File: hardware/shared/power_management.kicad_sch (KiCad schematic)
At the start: 32 parts, among them J3 FH12-12S-0.5SH(55), J4 1S Li-Po, Q1 AO3400A, U2 nPM1300-QEAA, U7 TPS63900DSKR

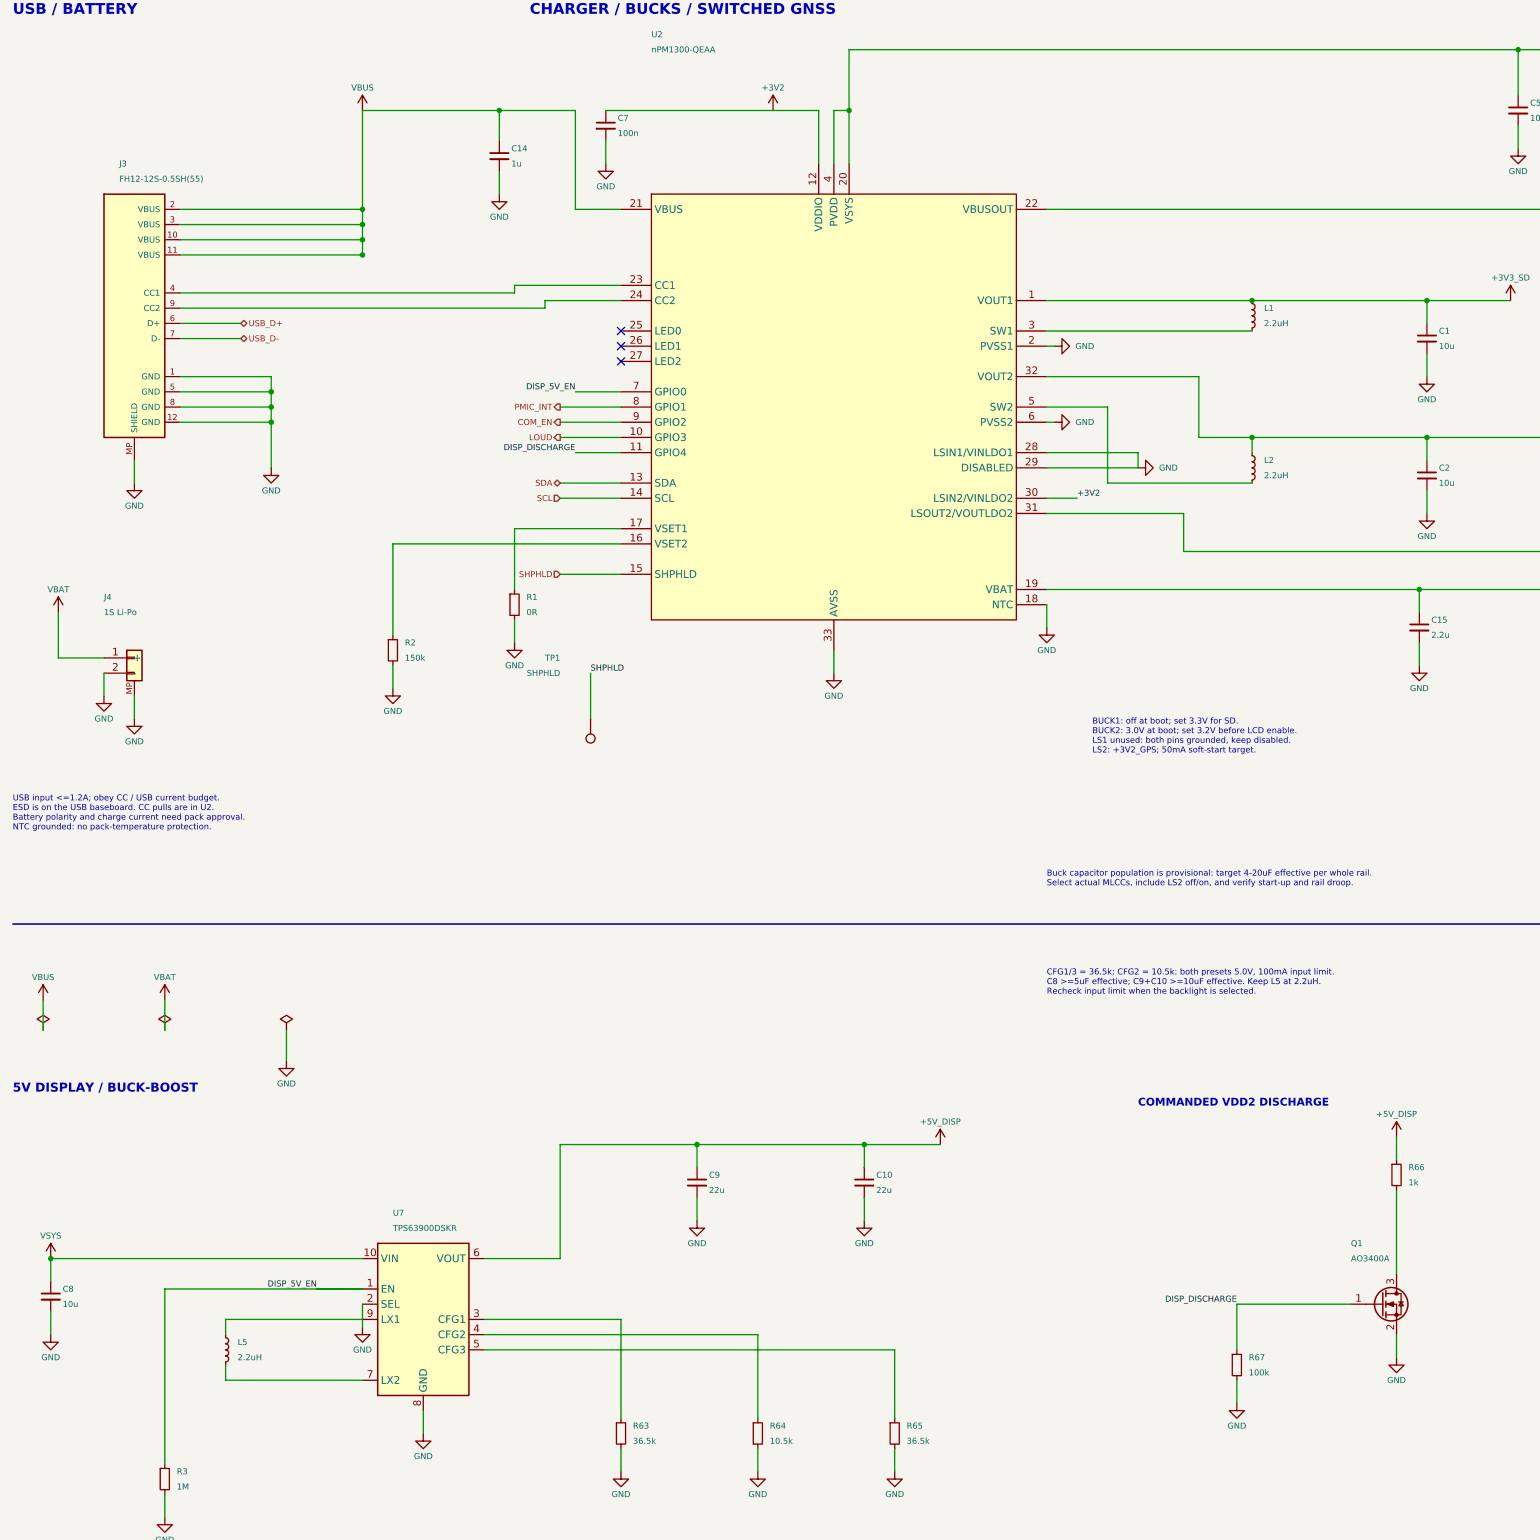
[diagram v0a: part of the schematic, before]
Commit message: hardware: tidy the QFN schematic layout and style
Layout pass on the eight sheets. ERC stays at 0 violations on OBC_PCB and
USB_Baseboard. A netlist comparison shows the same 127 net partitions and
the same components, values and footprints.

Root sheet
- Draw SCL, SDA, COM_EN, LOUD, SHPHLD, BTN_SELECT and BUZZER_PWM as label
  stubs. Wire crossings fall from 38 to 0.
- Redraw the DCC/DECD/DECA/DECRF network as a chain without crossings.
- Move R5 and C26 clear of the crystal wires. Use a ground symbol on Y1
  instead of a label named GND.
- Hang the I2C test points on the U6C stubs.

Power sheet
- Attach the VBUS, VBAT and GND power flags to their nets.
- Tap TP1 onto the SHPHLD wire.
- Use a +3V2 symbol on LSIN2 instead of a label.
- Route SW2, the VSET straps and the CFG resistors without crossings.
- Move the SEL ground away from the LX1 pin.
- Show LSOUT1(GND) and INT(GND) for the unused LS1 and BMP581 pins.

Display, GNSS, user I/O
- Move J1 pin VA below VB so the VCOM/VB link no longer crosses VA.
- Move the GNSS FTE labels clear of the antenna pin 3 wire.
- Straighten the piezo wiring. Put the GND probe pad above its ground
  symbol.

Style
- One heading size (1.8 bold), one sub-heading size (1.27 bold) and one
  note size (1.0).
- Hide the voltage, dielectric and tolerance fields on the GNSS and radio
  sheets. Remove their dashed frames. Move both sheets to the top-left.
- Use Rev QFN and the same title format on every sheet.
- Set TP1 and TP2 to in_bom no like the other probe pads.
- Add C21 to the VDD bypass note.

Net names change for five nets because their labels are now on the root
sheet: BTN_SELECT, BUZZER_PWM, COM_EN, LOUD and SHPHLD. No net class
pattern uses them.

Co-Authored-By: Claude Sonnet 5.5 <noreply@anthropic.com>
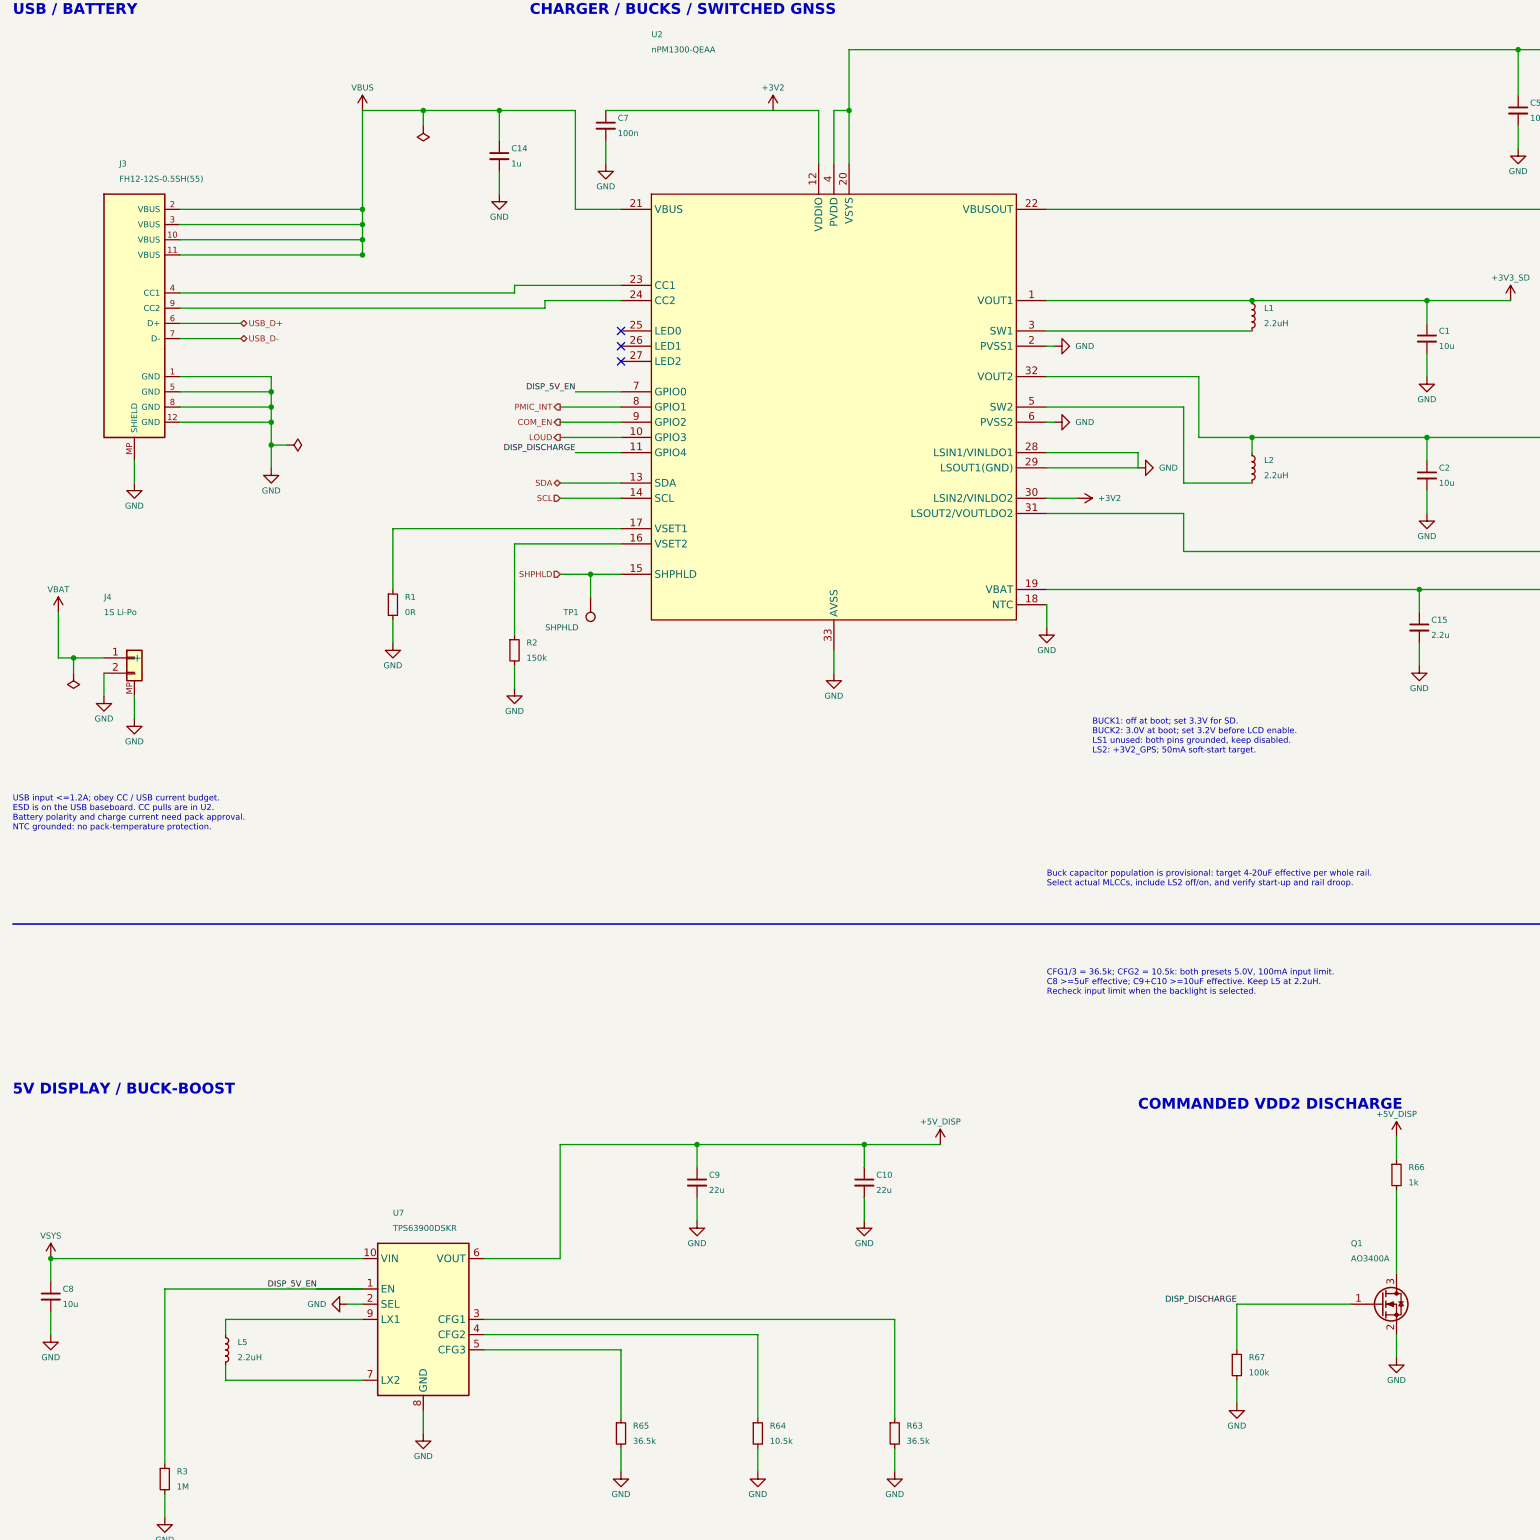
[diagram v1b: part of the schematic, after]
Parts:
- TP1: now left out of the parts list
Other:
- title: OpenBikeComputer - QFN power management -> OpenBikeComputer - power management
- moved on the sheet: R1, R2, R63, R65, TP1
